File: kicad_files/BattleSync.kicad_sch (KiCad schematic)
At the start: 14 parts, among them U1 113991054, U2 DFR0299, U3 AMS1117-3.3

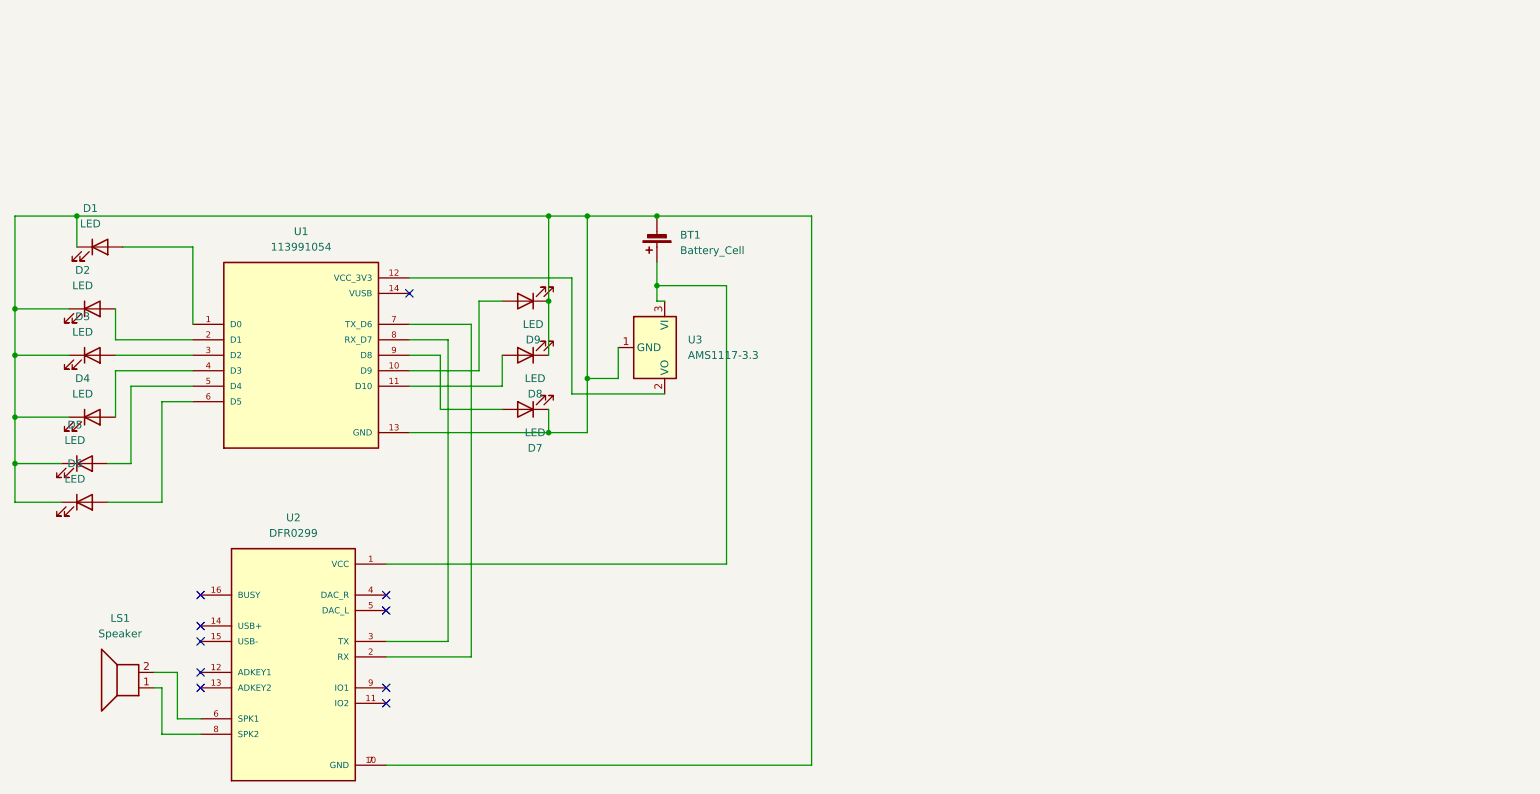
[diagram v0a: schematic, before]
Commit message: work on updating kicad files with project-level symbols and footprints
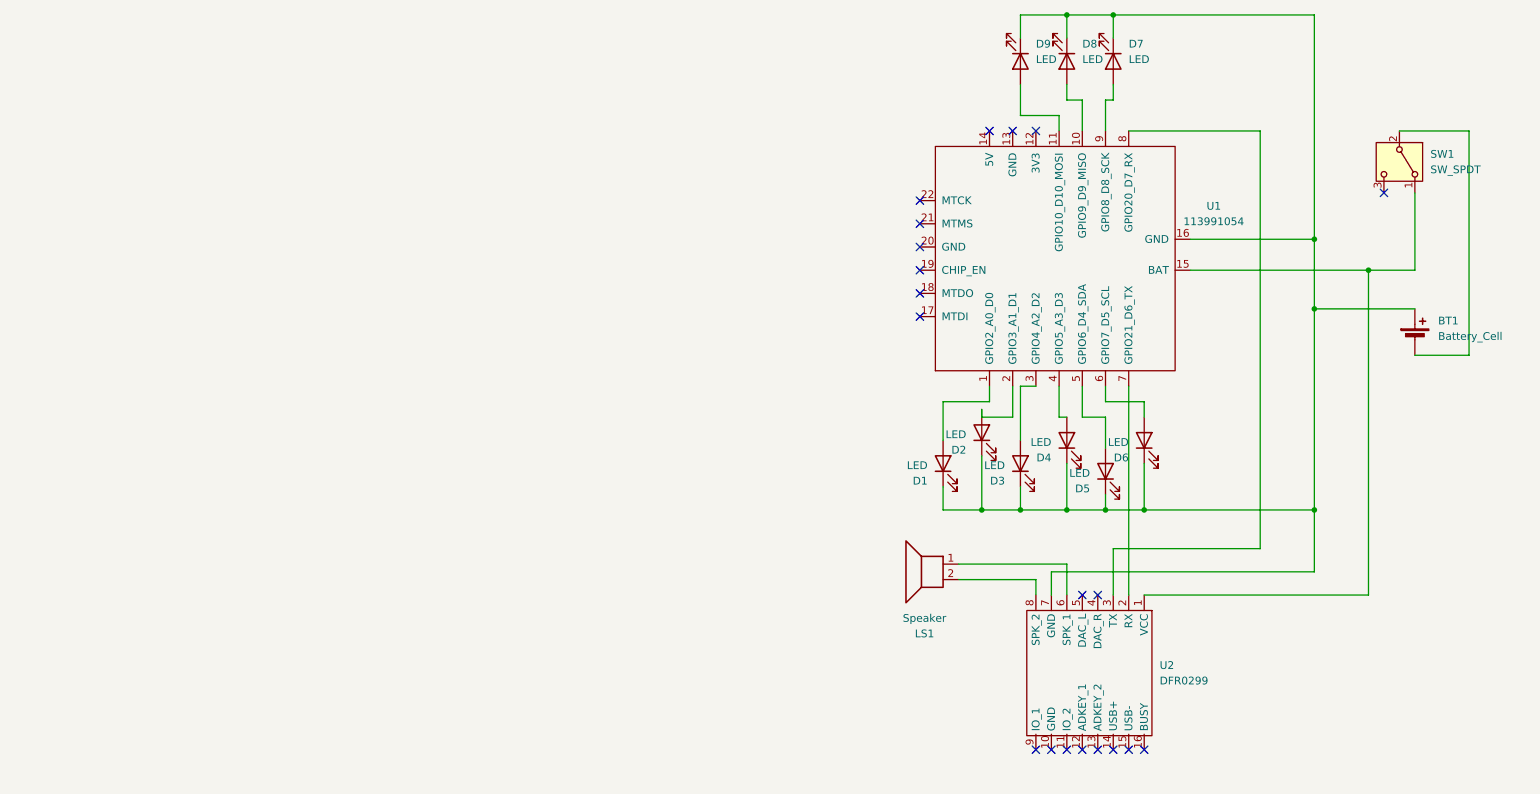
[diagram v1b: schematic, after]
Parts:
- removed U3: AMS1117-3.3, Package_TO_SOT_SMD:SOT-223-3_TabPin2, symbol Regulator_Linear:AMS1117-3.3
- added SW1: SW_SPDT, Connector_JST:JST_PH_B2B-PH-K_1x02_P2.00mm_Vertical, symbol Switch:SW_SPDT
- BT1, LS1: footprint Connector_JST:JST_XH_B2B-XH-A_1x02_P2.50mm_Vertical -> Connector_JST:JST_PH_B2B-PH-K_1x02_P2.00mm_Vertical
- D1, D2, D3, D4, D5, D6, D7, D8, D9: footprint Connector_Wire:SolderWire-1.5sqmm_1x02_P7.8mm_D1.7mm_OD3.9mm -> Connector_JST:JST_PH_B2B-PH-K_1x02_P2.00mm_Vertical
- U1: footprint 113991054:MODULE_113991054 -> Seeeduino xiao ESP32C3 KiCAD Library:MODULE_113991054; symbol 113991054:113991054 -> Seeed_Studio_XIAO_Series:XIAO-ESP32-C3-SMD
- U2: symbol DFR0299:DFR0299 -> DFPlayer:DFPlayer
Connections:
- net at LS1.1: now also U2.6 (SPK_1); no longer U2.8 (SPK2)
- net at LS1.2: now also U2.8 (SPK_2); no longer U2.6 (SPK1)
- net at D1.1 (K), D2.1 (K), D3.1 (K)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: now also BT1.1 (+), U1.16 (GND); no longer BT1.2 (-), U1.13 (GND), U2.10 (GND)
- net at U1.10 (GPIO9_D9_MISO): now also D8.2 (A); no longer D9.2 (A)
- net at U2.1 (VCC): now also U1.15 (BAT), SW1.1 (A); no longer BT1.1 (+)
- net at U1.11 (GPIO10_D10_MOSI): now also D9.2 (A); no longer D8.2 (A)
- new net: BT1.2 (-), SW1.2 (B)
- no-connect marks 10 -> 20
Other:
- moved on the sheet: BT1, LS1
